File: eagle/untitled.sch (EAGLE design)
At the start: 11 parts, among them U1 ESP-WROOM-32

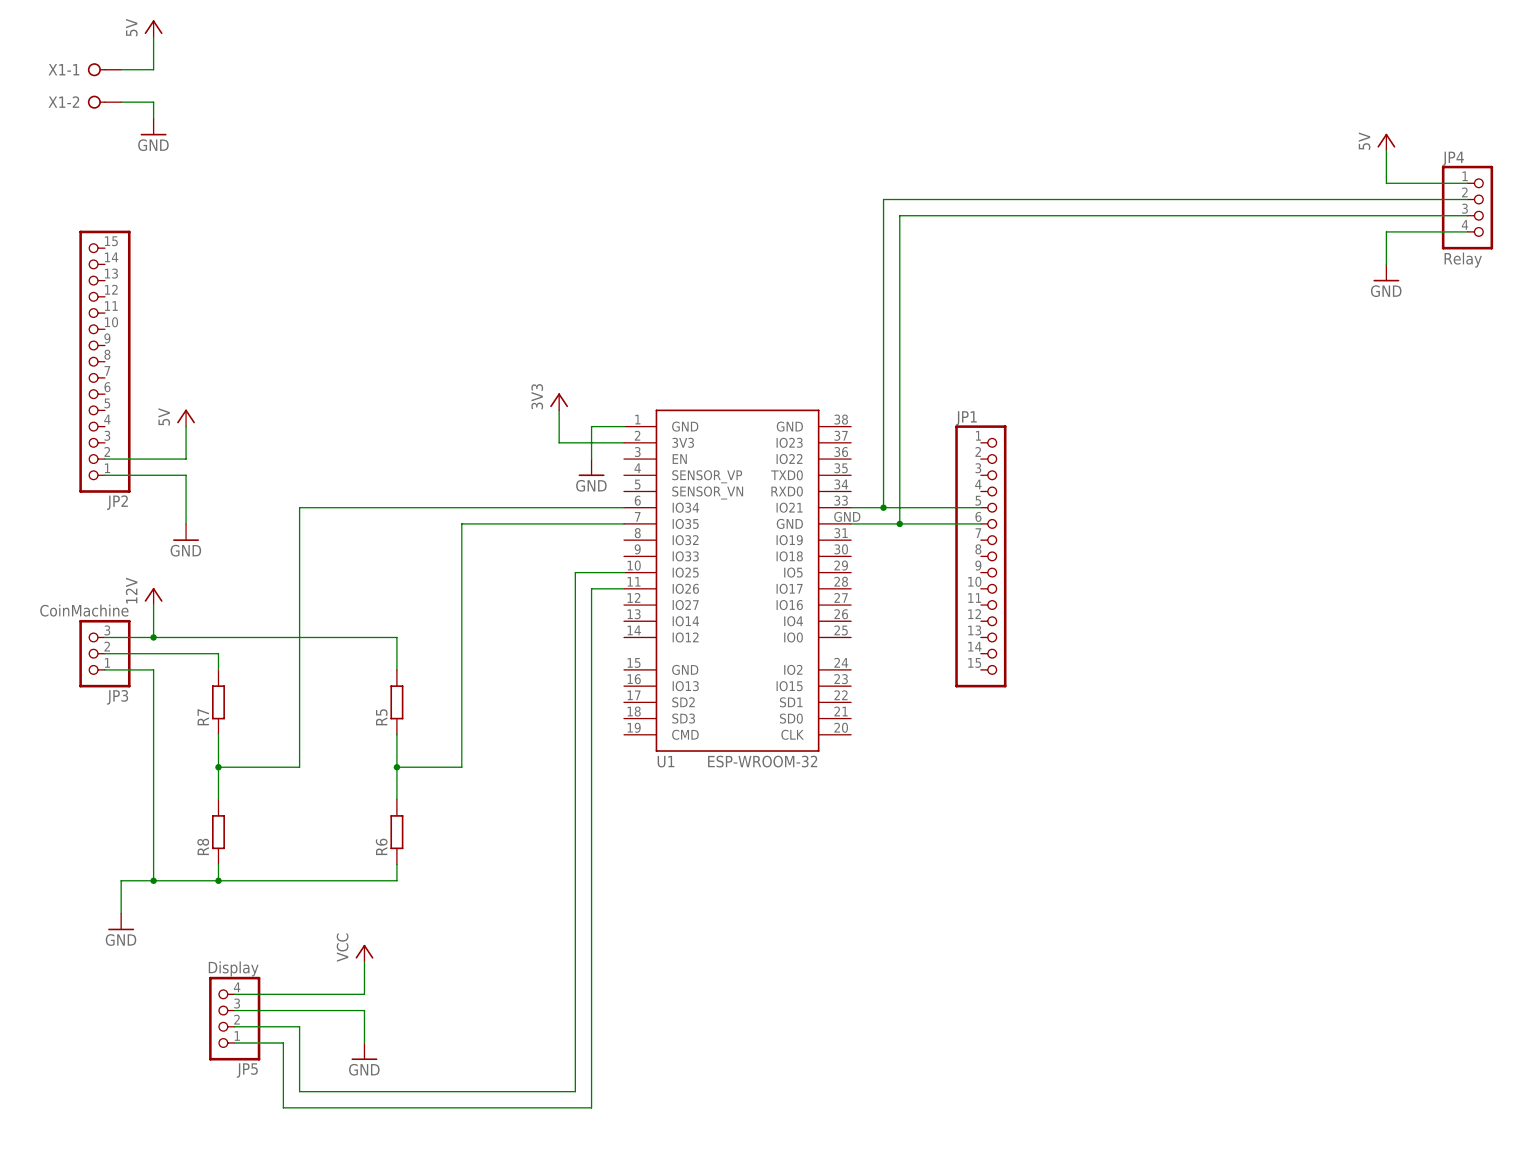
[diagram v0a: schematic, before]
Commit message: #Eagle - Change Arduino symbol
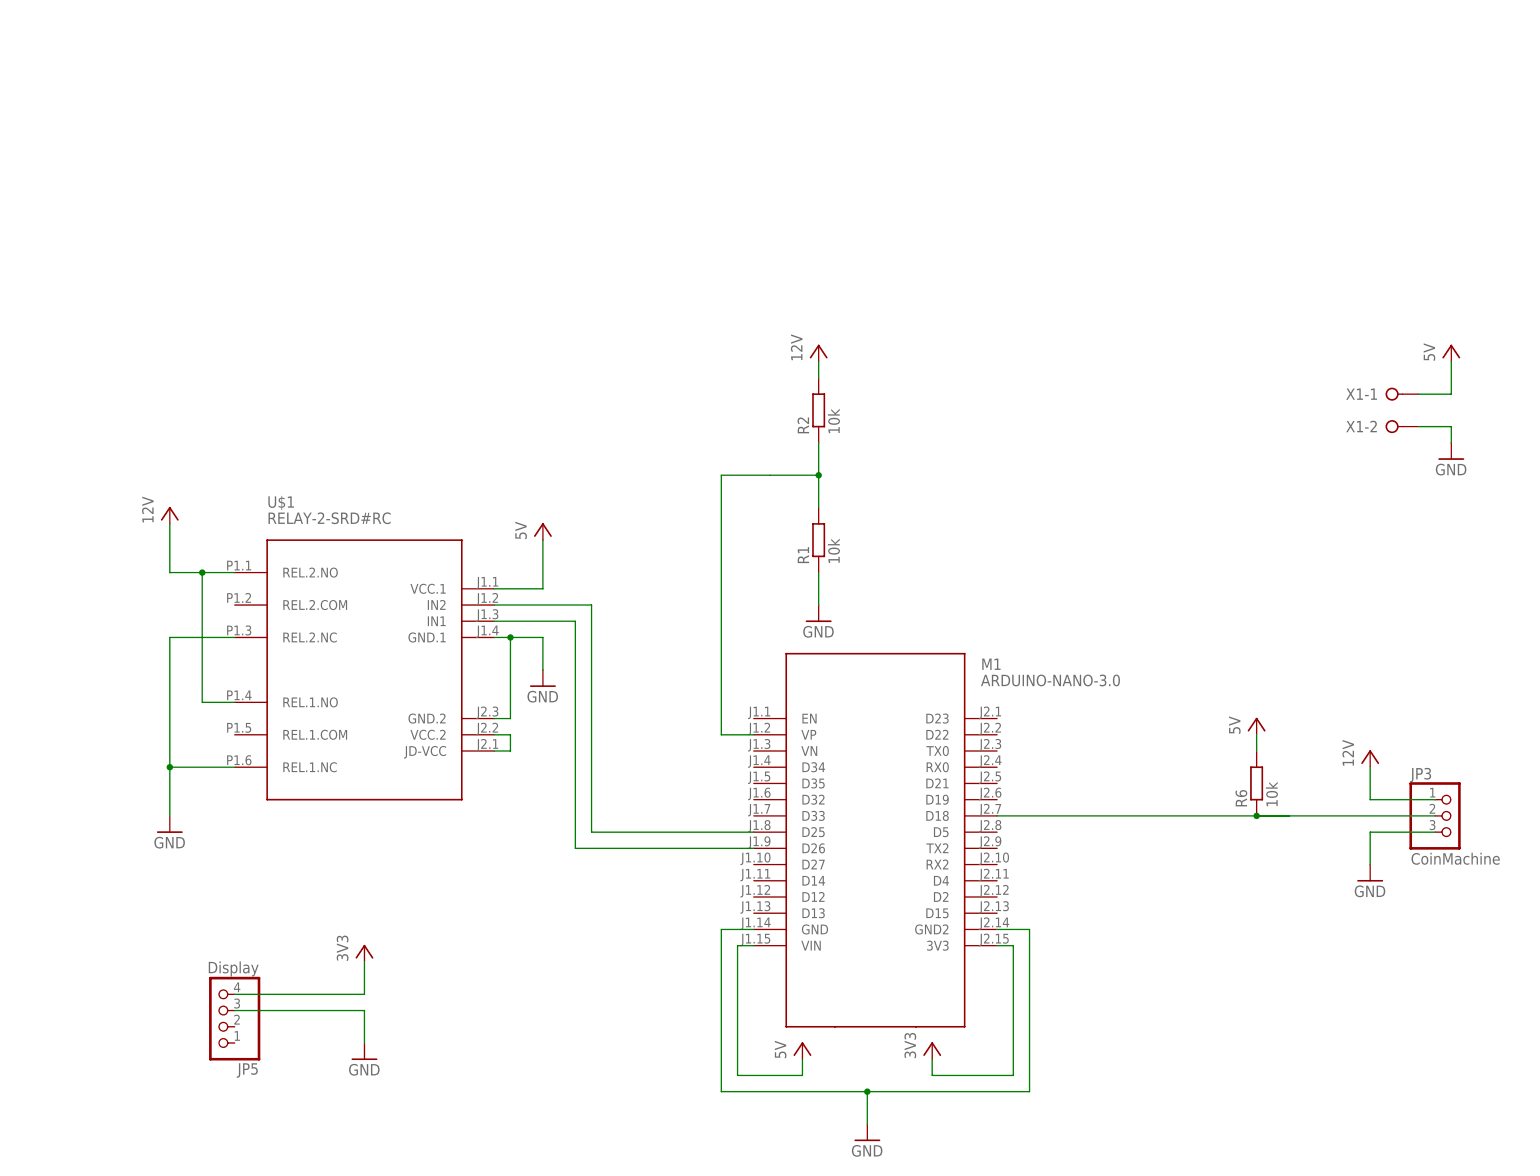
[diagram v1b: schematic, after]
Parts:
- removed JP1, JP2: (no value), pinhead:PINHD-1X15
- removed JP4: Relay, pinhead:PINHD-1X4
- removed R5, R7, R8: (no value), resistor:R-EU_0207/10
- removed U1: ESP-WROOM-32, esp32:ESP-WROOM-32
- added M1: ARDUINO-NANO-3.0, diy-modules:ARDUINO-NANO-3.0
- added R1, R2: 10k, resistor:R-EU_0207/10
- added U$1: RELAY-2-SRD#RC, diy-modules:RELAY-2-SRD#RC
- R6: value (none) -> 10k
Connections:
- removed net N$6: JP5.1, U1.IO26
- removed net N$8: JP5.2, U1.IO25
- net GND: now also JP3.3, M1.GND, M1.GND2, R1.1, U$1.GND.1, U$1.GND.2, U$1.REL.1.NC, U$1.REL.2.NC; no longer JP2.1, JP3.1, JP4.4, R6.1, R8.1, U1.GND@1
- net N$1: now also JP3.2, M1.D18, R6.1; no longer R7.1, R8.2, U1.IO34
- net N$2: now also M1.VP, R1.2, R2.1; no longer R5.1, R6.2, U1.IO35
- net N$3: now also M1.D25, U$1.IN2; no longer JP1.5, JP4.2, U1.IO21
- net N$4: now also M1.D26, U$1.IN1; no longer JP1.6, JP4.3, U1.GND@4
- net N$5: now also U$1.JD-VCC, U$1.VCC.2; no longer JP3.2, R7.2
- net VCC: now also JP3.1, M1.3V3, M1.VIN, R2.2, R6.2, U$1.REL.1.NO, U$1.REL.2.NO, U$1.VCC.1; no longer JP2.2, JP3.3, JP4.1, R5.2, U1.3V3
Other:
- moved on the sheet: JP3, R6, X1-1, X1-2
